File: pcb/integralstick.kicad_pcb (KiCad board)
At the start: 4 copper layers, 250 parts, among them J1 CONN_INTEGRALSTICK_FPGA_DEVICE, J2 CONN_INTEGRALSTICK_MCU_DEVICE, Q1 SSM6N58NU, Q2 SSM6N58NU, Q3 SSM6N58NU, U1 STM32F777NIH6‎, U10 DSC6083MI2A-032K768, U12 DSC6001HI2A-025.0000‎, U2 XC7A50T-1FTG256C, U3 S27KS0641, U4 S27KS0641, U5 KSZ9031RN, U6 S25FL064LABNFI011‎, U7 LTC3374-QFN, U8 DSC6001HI2A-025.0000, U9 AT24MAC402-UDFN

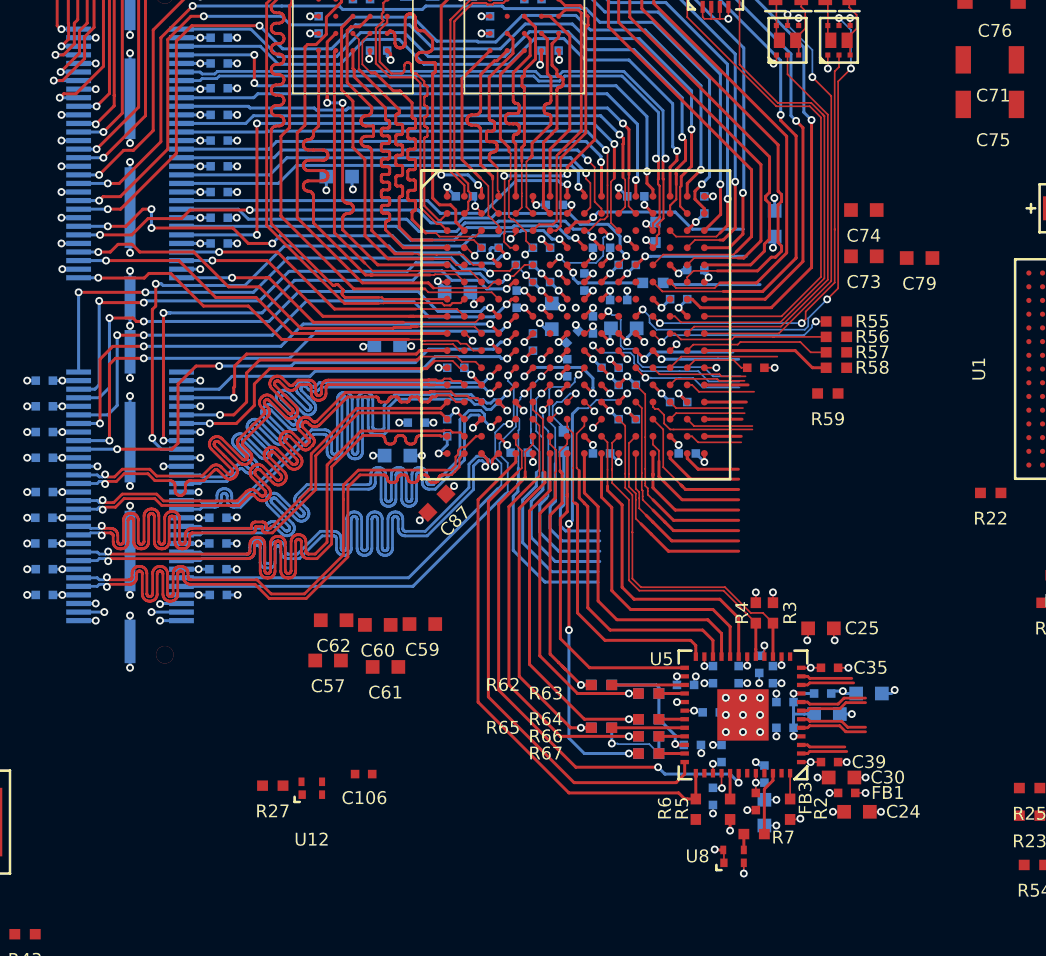
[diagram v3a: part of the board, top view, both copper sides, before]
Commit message: Fixed diffpair DRC issues
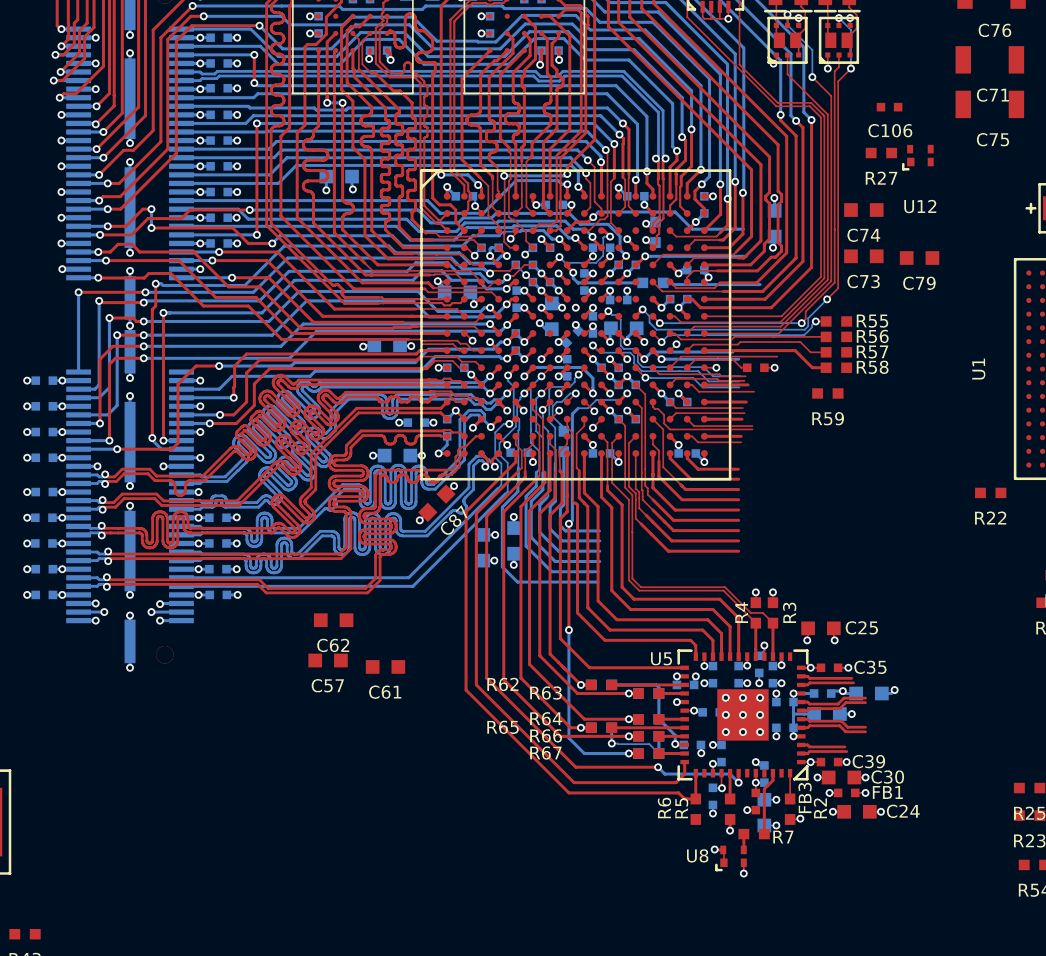
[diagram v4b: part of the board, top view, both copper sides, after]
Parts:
- C59, C60: moved to B.Cu
- moved R27 51.2 mm to (81.8, 33.0)
- moved U12 51.2 mm to (84.1, 33.1)
- moved C106 49.5 mm to (82.3, 30.3)
- moved C60 9.34 mm to (60.4, 55.6), turned to 90 degrees
- moved C59 5.69 mm to (58.6, 56.0), turned to 90 degrees
- moved C67 1.00 mm to (60.5, 44.0)
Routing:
- net /1V0: track 33.4 -> 48.5 mm, vias 11 -> 13
- net /GND: track 525.4 -> 532.1 mm, vias 135 -> 137
- net /MCU/DCMI_D7: track 15.9 -> 17.4 mm
- net /Ethernet/RGMII_RST_N: track 32.4 -> 33.0 mm
- net /Ethernet/RGMII_MDC: track 30.6 -> 31.2 mm
- net /Ethernet/RGMII_MDIO: track 32.0 -> 32.5 mm
- net /FPGA/LVDS_DQ7_N: track 37.3 -> 37.8 mm
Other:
- net class Default: clearance 0.1 -> 0.099
- rule trace_clearance: 0.1 -> 0.099

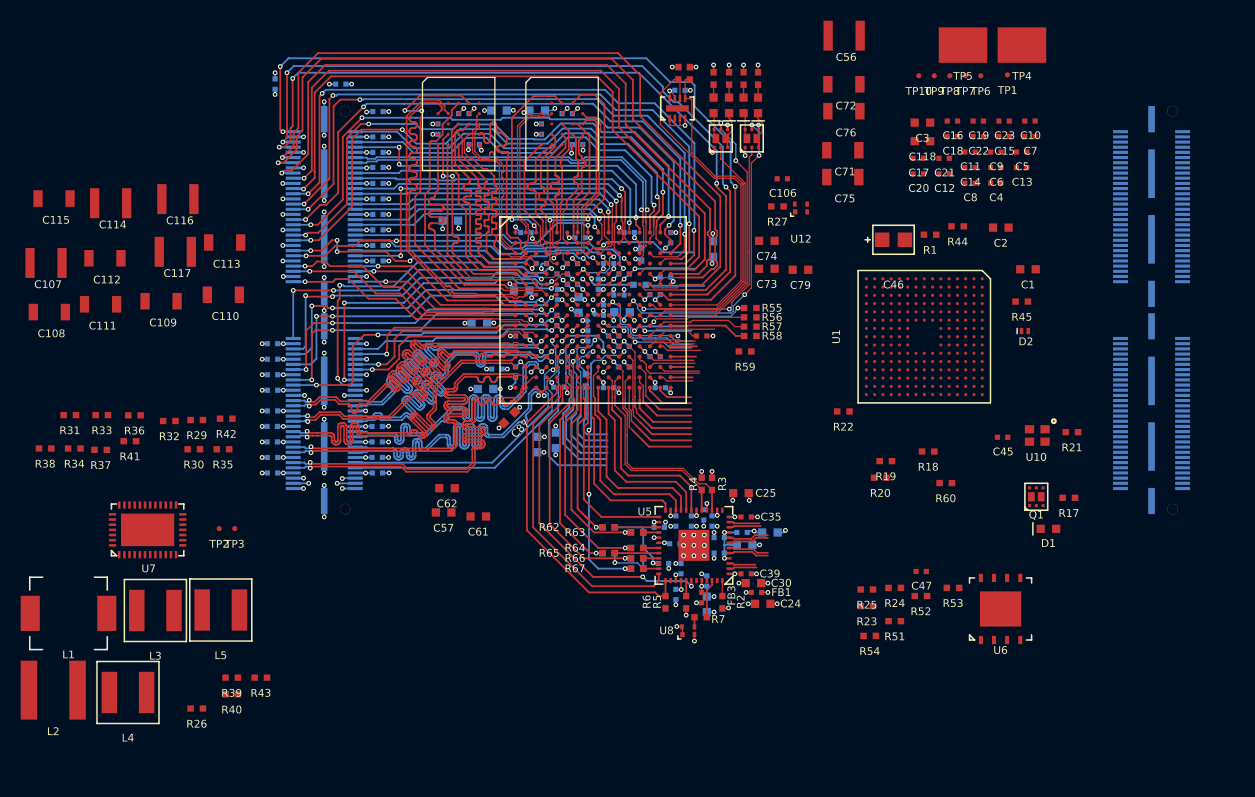
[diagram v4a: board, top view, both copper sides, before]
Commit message: Initial placement of SMPS and inductors. No caps.
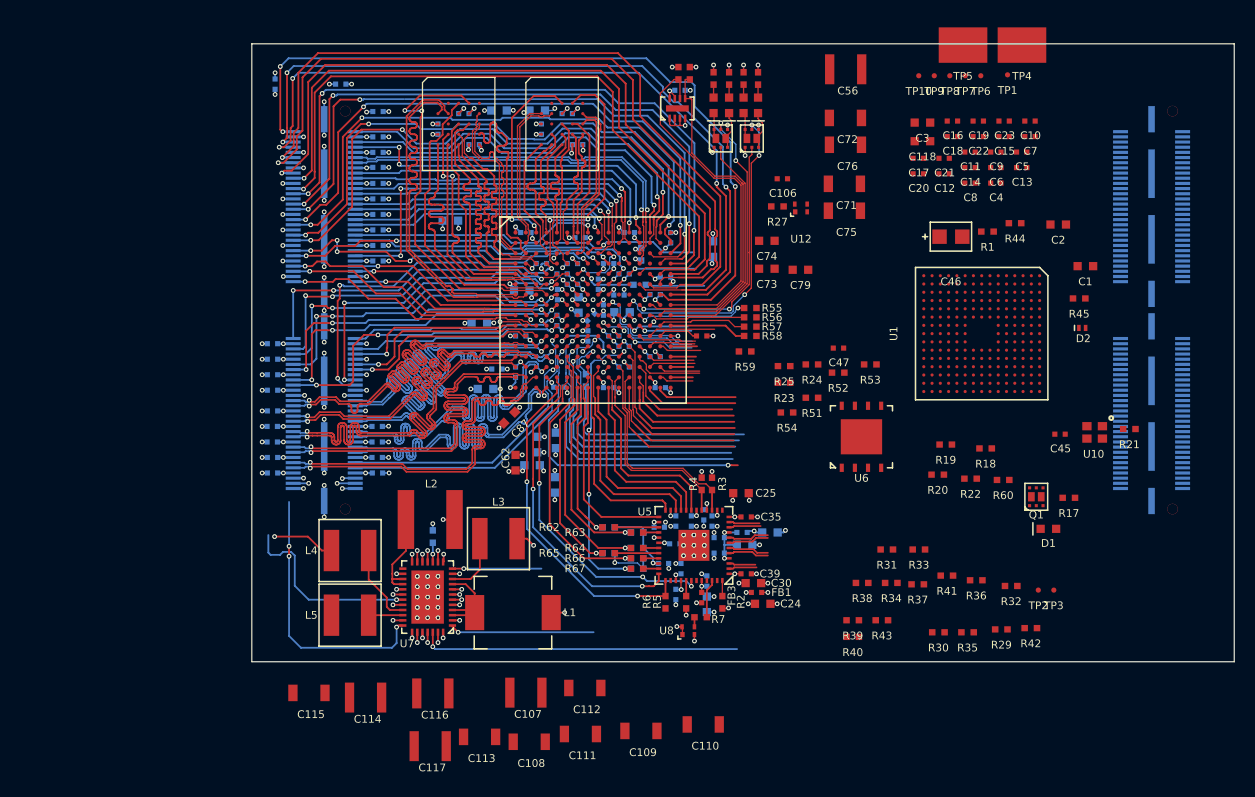
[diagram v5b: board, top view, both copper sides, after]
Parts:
- C57, C61, R26: moved to B.Cu
- moved R32 82.9 mm to (104.4, 69.7)
- moved R36 82.9 mm to (101.0, 69.1)
- moved R42 80.4 mm to (106.3, 73.8)
- moved R29 80.4 mm to (103.5, 73.9)
- moved R31 80.1 mm to (92.4, 66.2)
- moved R33 80.1 mm to (95.5, 66.2)
- moved R34 80.1 mm to (92.8, 69.4)
- moved R37 80.1 mm to (95.4, 69.5)
- moved R38 80.1 mm to (90.0, 69.4)
- moved R41 80.1 mm to (98.2, 68.7)
- moved TP2 79.4 mm to (107.0, 70.1)
- moved TP3 79.4 mm to (108.5, 70.1)
- moved R30 74.1 mm to (97.4, 74.2)
- moved R35 74.1 mm to (100.2, 74.2)
- moved C108 62.3 mm to (57.8, 84.7)
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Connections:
- U7 pad 10: /Power Supply/3V3_SW -> /Power Supply/1V2_SW
- U7 pad 12: /Power Supply/3V3_FB -> /Power Supply/1V2_FB
- U7 pad 18: /Power Supply/5V0 -> /GND
- U7 pad 19: /GND -> /Power Supply/5V0
- U7 pad 20: /Power Supply/5V0 -> /Power Supply/3V3_FB
- U7 pad 23: /Power Supply/1V2_SW -> /Power Supply/3V3_SW
- U7 pad 25: /Power Supply/1V2_FB -> /Power Supply/5V0
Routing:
- net /Power Supply/5V0: track 14.3 -> 83.0 mm, vias 6 -> 25
- net /GND: track 532.1 -> 590.0 mm, vias 137 -> 159
- net /1V2: track 30.0 -> 65.1 mm, vias 8 -> 9
- net /3V3: track 218.1 -> 252.7 mm, vias 51 -> 53
- net /PSU_TEMP: track 11.1 -> 42.1 mm, vias 1 -> 2
- net /Power Supply/2V5_FB: track 0.00 -> 26.2 mm, vias 0 -> 3
- net /1V0: track 48.5 -> 74.4 mm, vias 13 -> 17
- net /1V8: track 166.1 -> 187.7 mm, vias 32 -> 33
- net /Power Supply/1V8_FB: track 0.00 -> 18.5 mm, vias 0 -> 1
- net /RAM/GPIO_1V8_7: track 2.58 -> 17.6 mm, vias 0 -> 1
- net /Power Supply/1V0_FB: track 0.00 -> 14.0 mm, vias 0 -> 1
- net /FPGA_TDO: track 6.81 -> 20.0 mm
- net /MCU/DCMI_D7: track 17.4 -> 30.1 mm, vias 1 -> 2
- net /FPGA_RST_N: track 14.4 -> 27.1 mm
- net /FPGA_TDI: track 12.1 -> 24.3 mm
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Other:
- board outline added: 95 x 59.8 mm

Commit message: Continued work on layout. Added some layer crossing caps. Initial power plane placement.
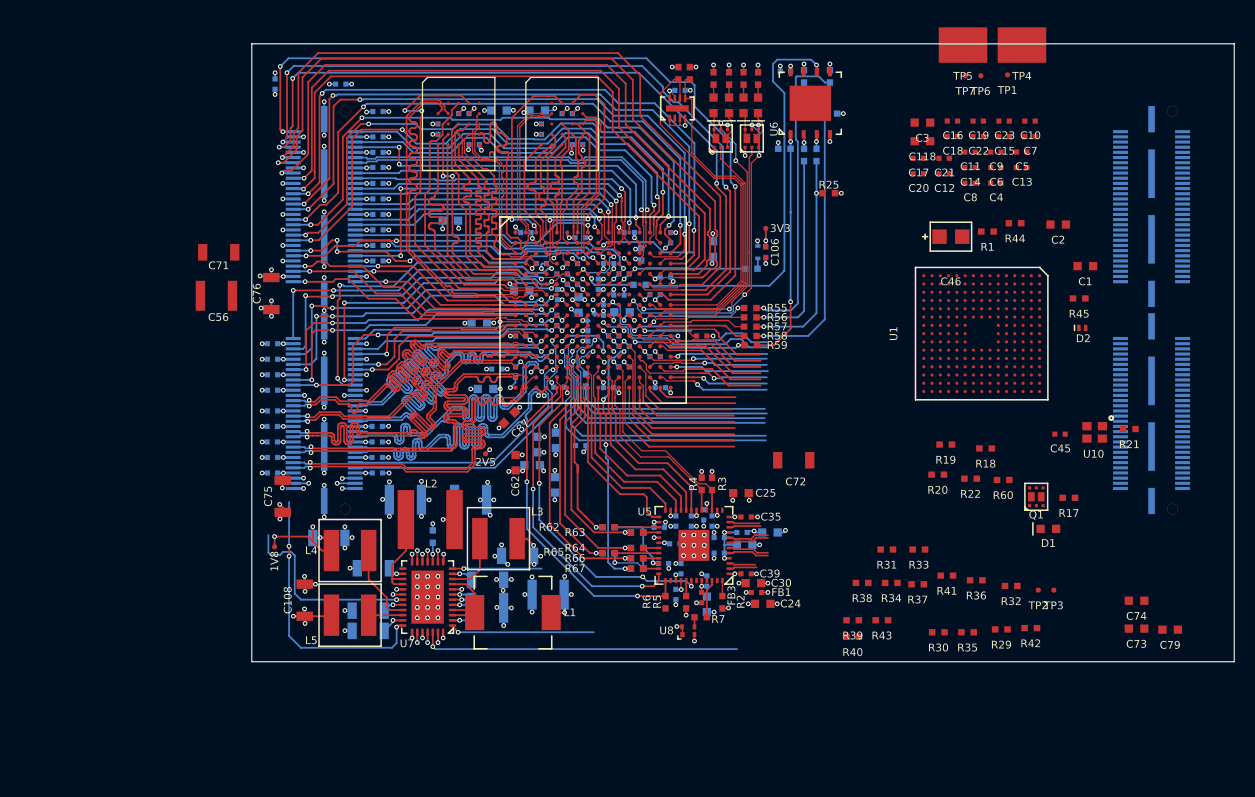
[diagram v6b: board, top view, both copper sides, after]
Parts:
- added C144: 0.47 uF, azonenberg_pcb:EIA_0402_CAP_NOSILK, B.Cu at (62.8, 56.1)
- C107, C109, C110, C111, C112, C113, C114, C115, C116, C117, C47, R23, R24, R27, R51, R52, R53, R54, U12: moved to B.Cu
- moved TP8 79.6 mm to (33.2, 65.9)
- moved C56 64.7 mm to (27.6, 41.6)
- moved C75 60.9 mm to (34.0, 61.0), turned to 270 degrees
- moved C71 60.9 mm to (27.8, 37.4)
- moved C76 57.3 mm to (32.9, 41.4), turned to 270 degrees
- moved TP9 56.7 mm to (53.6, 56.9)
- moved C79 49.9 mm to (119.8, 73.9)
- moved C73 49.9 mm to (116.5, 73.8)
- moved C74 49.9 mm to (116.5, 71.1)
- moved C110 40.4 mm to (38.5, 65.0)
- moved C72 33.5 mm to (83.4, 57.5)
- moved R54 32.8 mm to (86.9, 20.4), turned to 90 degrees
- moved U6 32.6 mm to (85.0, 23.0)
- moved C109 30.3 mm to (42.8, 68.0), turned to 180 degrees
- moved R53 28.6 mm to (84.4, 20.4), turned to 90 degrees
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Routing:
- net /GND: track 590.0 -> 732.6 mm, vias 159 -> 195
- net /3V3: track 252.7 -> 292.3 mm, vias 53 -> 60
- net /QSPI_CLK: track 5.69 -> 39.8 mm, vias 0 -> 1
- net /MCU/QSPI_DQ3: track 0.00 -> 32.3 mm, vias 0 -> 1
- net /MCU/QSPI_DQ0: track 0.00 -> 29.9 mm, vias 0 -> 1
- net /MCU/QSPI_CS_N: track 0.00 -> 22.8 mm, vias 0 -> 2
- net /MCU/QSPI_DQ2: track 0.00 -> 21.6 mm, vias 0 -> 2
- net /MCU/QSPI_DQ1: track 0.00 -> 19.4 mm, vias 0 -> 1
- net /Power Supply/5V0: track 83.0 -> 102.2 mm, vias 25 -> 28
- net /2V5: track 146.5 -> 161.8 mm, vias 20 -> 25
- net /1V8: track 187.7 -> 199.7 mm, vias 33 -> 37
- net /FPGA/FPGA_INIT: track 10.3 -> 18.2 mm
- net /FPGA_DONE: track 11.0 -> 18.9 mm
- net /MCU/DCMI_VSYNC: track 3.29 -> 10.8 mm, vias 0 -> 1
- net Net-(R22-Pad1): track 2.15 -> 9.55 mm, vias 0 -> 1
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- added copper zone on In2.Cu, net /1V2
- added copper zone on In2.Cu, net /Ethernet/A2V5
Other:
- board text added: "1V8"
- board text added: "2V5"
- board text added: "3V3"

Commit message: Initial STM32 fanout
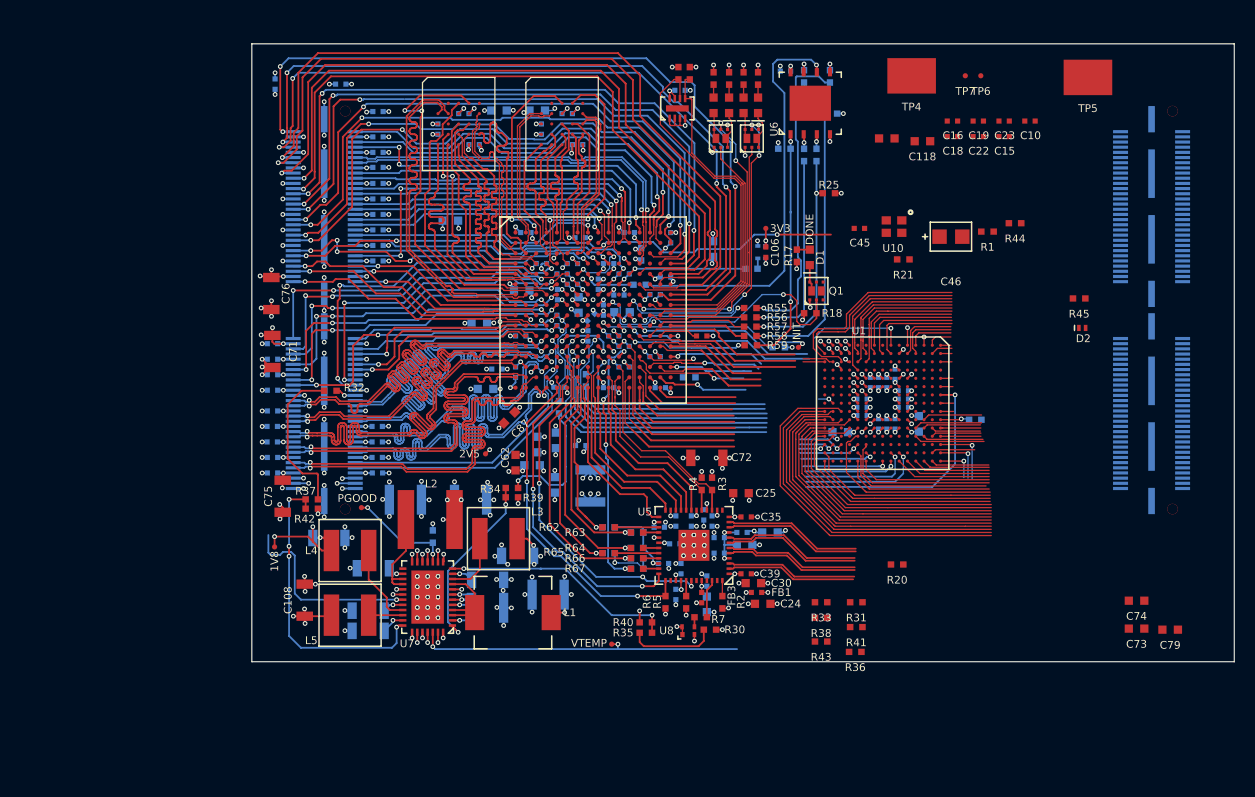
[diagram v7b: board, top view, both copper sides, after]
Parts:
- C1, C11, C12, C13, C14, C17, C2, C20, C21, C4, C5, C56, C6, C7, C8, C9, R19, R22, R29, R60: moved to B.Cu
- moved R42 70.5 mm to (36.8, 62.2), turned to 180 degrees
- moved R32 68.5 mm to (38.6, 50.8)
- moved TP2 65.9 mm to (41.6, 62.1)
- moved R37 59.2 mm to (36.8, 61.3)
- moved R29 47.9 mm to (60.7, 52.4), turned to 90 degrees
- moved TP3 43.1 mm to (65.8, 75.3)
- moved C56 40.6 mm to (63.8, 60.0), turned to 90 degrees
- moved R34 37.8 mm to (56.1, 60.2)
- moved R17 35.2 mm to (83.7, 37.8), turned to 90 degrees
- moved R39 35.0 mm to (56.1, 61.1), turned to 180 degrees
- moved D1 35.0 mm to (85.0, 37.9), turned to 90 degrees
- moved TP1 33.2 mm to (83.8, 46.6)
- moved R35 31.1 mm to (69.1, 74.2), turned to 180 degrees
- moved Q1 29.1 mm to (85.6, 41.1)
- moved R22 28.9 mm to (73.3, 49.5)
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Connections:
- J2 pad 118: /Ethernet/ETH_A_N -> /JTAG_TMS
- J2 pad 120: /Ethernet/ETH_A_P -> /MCU_TDO
- J2 pad 4: /JTAG_TMS -> /Ethernet/ETH_A_P
- J2 pad 6: /MCU_TDO -> /Ethernet/ETH_A_N
- U2 pad K12: /MCU/SPI5_MOSI -> /MCU/RMII_REFCLK
- U2 pad K13: /MCU/RMII_MDC -> /MCU/RMII_MDIO
- U2 pad L13: /MCU/RMII_MDIO -> /MCU/RMII_RXD0
- U2 pad L14: /MCU/RMII_TXD0 -> /MCU/RMII_CRS_DV
- U2 pad M12: /MCU/RMII_CRS_DV -> /MCU/RMII_TXD0
- U2 pad M14: /MCU/RMII_TXD1 -> /MCU/RMII_RXD1
- U2 pad M16: /MCU/RMII_RXD0 -> /MCU/RMII_TXD1
- U2 pad N14: /MCU/RMII_REFCLK -> /MCU/SPI5_MOSI
- U2 pad N16: /MCU/RMII_RXD1 -> /MCU/RMII_MDC
- U2 pad P14: /MCU/DCMI_D3 -> /MCU/DCMI_PIXCLK
- U2 pad P16: /MCU/DCMI_HSYNC -> /MCU/DCMI_D3
- U2 pad R12: /MCU/DCMI_PIXCLK -> /MCU/DCMI_HSYNC
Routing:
- net /3V3: track 292.3 -> 393.5 mm, vias 60 -> 92
- net /GND: track 732.6 -> 821.5 mm, vias 195 -> 228
- net Net-(J2-Pad83): track 0.00 -> 34.9 mm
- net Net-(J2-Pad87): track 0.00 -> 32.1 mm
- net Net-(J2-Pad84): track 0.00 -> 32.0 mm
- net Net-(J2-Pad88): track 0.00 -> 31.0 mm
- net Net-(J2-Pad64): track 0.00 -> 29.8 mm
- net Net-(J2-Pad65): track 0.00 -> 29.7 mm
- net Net-(J2-Pad89): track 0.00 -> 29.1 mm
- net Net-(J2-Pad66): track 0.00 -> 26.6 mm
- net Net-(J2-Pad94): track 0.00 -> 26.0 mm
- net Net-(J2-Pad93): track 0.00 -> 25.9 mm
- net /MCU/SPI5_MISO: track 0.80 -> 25.6 mm, vias 1 -> 2
- net /MCU/DCMI_D6: track 9.04 -> 32.4 mm, vias 0 -> 1
- net Net-(J2-Pad90): track 0.00 -> 23.0 mm
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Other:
- board text added: "DONE"
- board text added: "INIT"
- board text added: "PGOOD"
- board text added: "VTEMP"
